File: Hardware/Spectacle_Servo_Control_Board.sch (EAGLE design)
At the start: 39 parts, among them J1 FTDI_DEVICE, J10 AUDIO-JACK3, J3 USB-MICROB, J4 AUDIO-JACK3, U1 CY8C4146LQI-S422, U2 3.3V/150mA

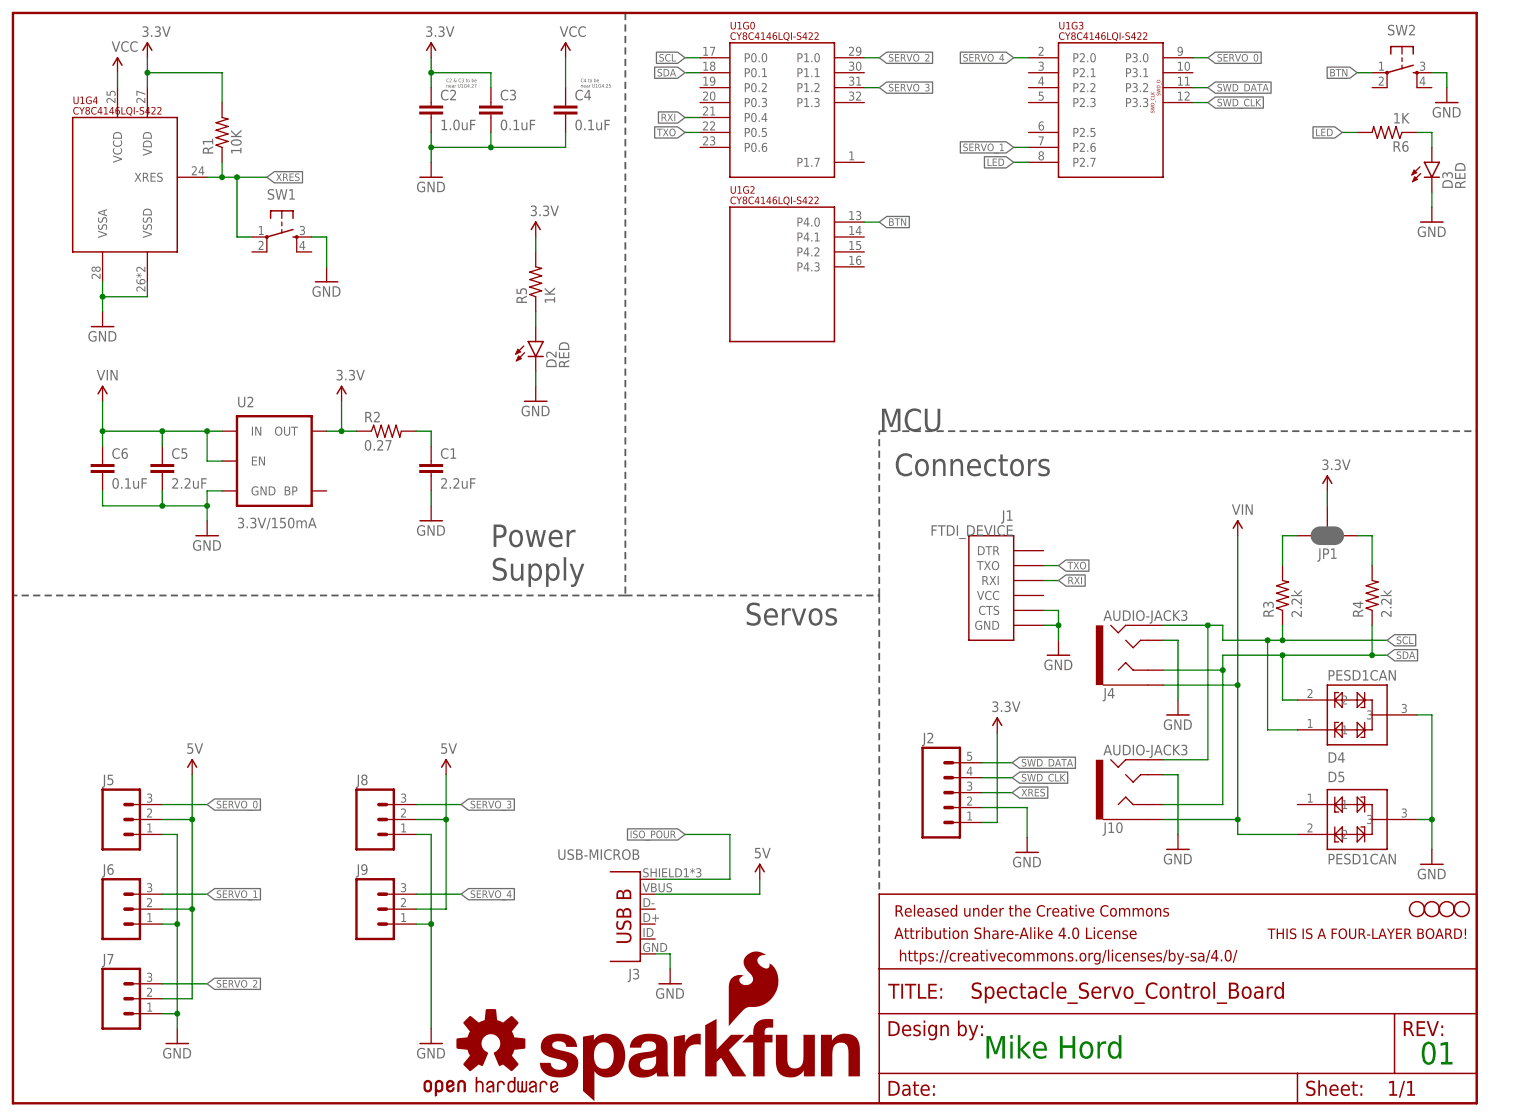
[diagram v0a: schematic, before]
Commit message: Changes from design review, initial checklist pass
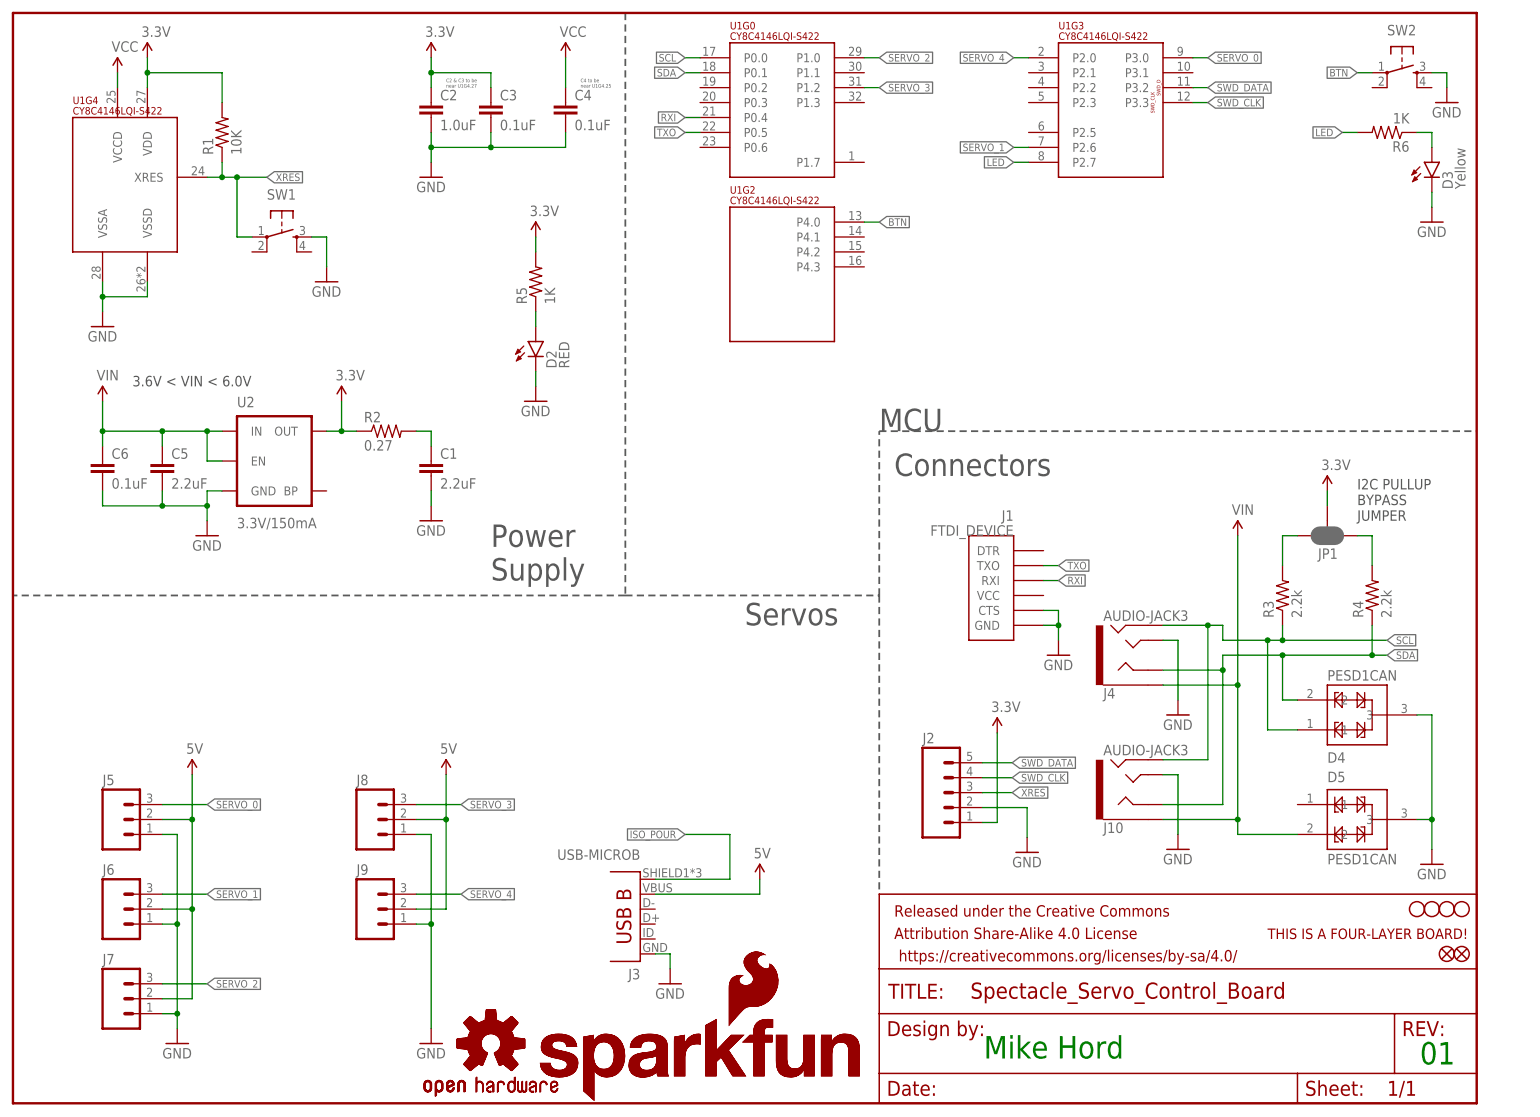
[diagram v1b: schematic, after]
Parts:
- added FD1, FD2: FIDUCIALUFIDUCIAL, SparkFun-Aesthetics:FIDUCIALUFIDUCIAL
- added LOGO3: SFE_LOGO_NAME_FLAME.1_INCH, SparkFun-Aesthetics:SFE_LOGO_NAME_FLAME.1_INCH
- added LOGO4: OSHW-LOGOS, SparkFun-Aesthetics:OSHW-LOGOS
- D3: value RED -> Yellow; device SparkFun-LED:LED-RED0603 -> SparkFun-LED:LED-YELLOW0603-SMART
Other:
- note added: "3.6V < VIN < 6.0V"
- note added: "I2C PULLUP BYPASS JUMPER"
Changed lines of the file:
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@@
 <part name="SW1" library="SparkFun-Electromechanical" deviceset="SWITCH_SPST_4_PIN" device="RECT"/>
 <part name="SW2" library="SparkFun-Electromechanical" deviceset="SWITCH_SPST_4_PIN" device="RECT"/>
-<part name="D3" library="SparkFun-LED" deviceset="LED-RED" device="0603" value="RED"/>
+<part name="D3" library="SparkFun-LED" deviceset="LED-YELLOW" device="0603-SMART" value="Yellow"/>
 <part name="R5" library="SparkFun-Resistors" deviceset="1KOHM-1/10W-1%(0603)" device="" value="1K"/>
 <part name="GND12" library="SparkFun-Aesthetics" deviceset="GND" device=""/>
@@
 <part name="J10" library="SparkFun-Connectors" deviceset="AUDIO-JACK3" device=""/>
 <part name="GND16" library="SparkFun-Aesthetics" deviceset="GND" device=""/>
+<part name="LOGO3" library="SparkFun-Aesthetics" deviceset="SFE_LOGO_NAME_FLAME" device=".1_INCH"/>
+<part name="LOGO4" library="SparkFun-Aesthetics" deviceset="OSHW-LOGO" device="S"/>
+<part name="FD1" library="SparkFun-Aesthetics" deviceset="FIDUCIAL" device="UFIDUCIAL"/>
+<part name="FD2" library="SparkFun-Aesthetics" deviceset="FIDUCIAL" device="UFIDUCIAL"/>
 </parts>
 <sheets>
@@
 <text x="81.28" y="88.9" size="3.81" layer="97" font="vector">Power
 Supply</text>
+<text x="20.32" y="121.92" size="1.778" layer="97">3.6V &lt; VIN &lt; 6.0V</text>
+<text x="228.6" y="99.06" size="1.778" layer="97">I2C PULLUP
+BYPASS
+JUMPER</text>
 </plain>
 <instances>
@@
 <instance part="J10" gate="G$1" x="190.5" y="53.34" rot="MR180"/>
 <instance part="GND16" gate="1" x="198.12" y="43.18"/>
+<instance part="LOGO3" gate="G$1" x="88.9" y="0"/>
+<instance part="LOGO4" gate="G$1" x="81.28" y="10.16"/>
+<instance part="FD1" gate="G$1" x="246.38" y="25.4"/>
+<instance part="FD2" gate="G$1" x="243.84" y="25.4"/>
 </instances>
 <busses>

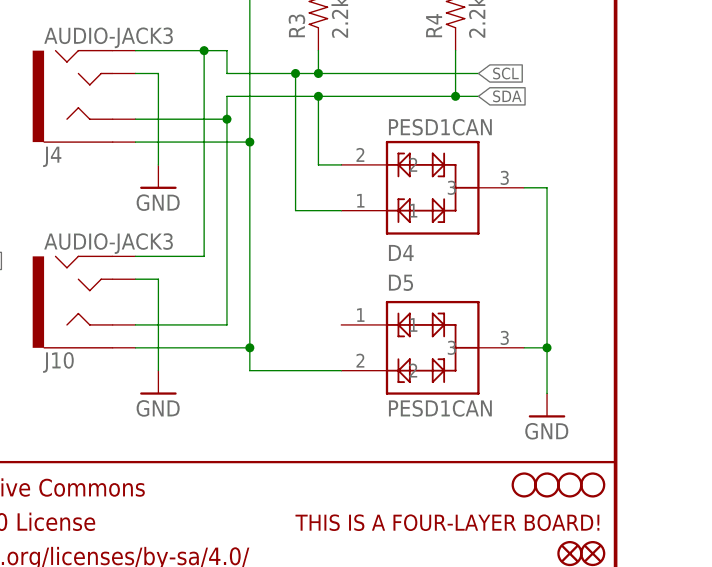
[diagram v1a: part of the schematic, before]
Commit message: Revised from feedback from QC
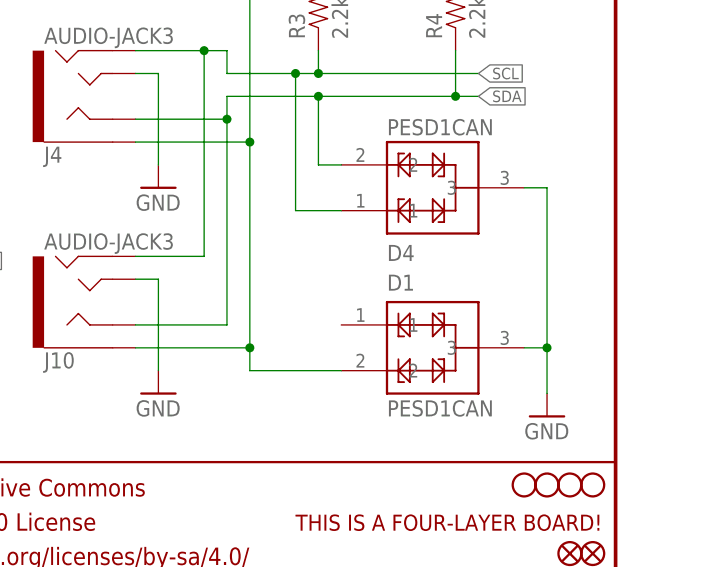
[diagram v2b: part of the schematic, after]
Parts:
- J10, J4: PROD_ID (none) -> CONN-10676
- renumbered D5 to D1
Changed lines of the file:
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@@
 <part name="SUPPLY9" library="SparkFun-Aesthetics" deviceset="3.3V" device=""/>
 <part name="SUPPLY11" library="SparkFun-Aesthetics" deviceset="3.3V" device=""/>
-<part name="J4" library="SparkFun-Connectors" deviceset="AUDIO-JACK3" device=""/>
+<part name="J4" library="SparkFun-Connectors" deviceset="AUDIO-JACK3" device="">
+<attribute name="PROD_ID" value="CONN-10676"/>
+</part>
 <part name="D4" library="SparkFun-DiscreteSemi" deviceset="PESD1CAN" device=""/>
 <part name="GND4" library="SparkFun-Aesthetics" deviceset="GND" device=""/>
-<part name="D5" library="SparkFun-DiscreteSemi" deviceset="PESD1CAN" device=""/>
+<part name="D1" library="SparkFun-DiscreteSemi" deviceset="PESD1CAN" device=""/>
 <part name="SUPPLY1" library="SparkFun-Aesthetics" deviceset="3.3V" device=""/>
 <part name="H1" library="SparkFun-Electromechanical" deviceset="STAND-OFF" device=""/>
@@
 <part name="LOGO1" library="SparkFun-Aesthetics" deviceset="OSHW-LOGO" device="S"/>
 <part name="LOGO2" library="SparkFun-Aesthetics" deviceset="SFE_LOGO_NAME_FLAME" device=".1_INCH"/>
-<part name="J10" library="SparkFun-Connectors" deviceset="AUDIO-JACK3" device=""/>
+<part name="J10" library="SparkFun-Connectors" deviceset="AUDIO-JACK3" device="">
+<attribute name="PROD_ID" value="CONN-10676"/>
+</part>
 <part name="GND16" library="SparkFun-Aesthetics" deviceset="GND" device=""/>
 <part name="LOGO3" library="SparkFun-Aesthetics" deviceset="SFE_LOGO_NAME_FLAME" device=".1_INCH"/>
@@
 <instance part="SUPPLY9" gate="G$1" x="55.88" y="119.38"/>
 <instance part="SUPPLY11" gate="G$1" x="223.52" y="104.14"/>
-<instance part="J4" gate="G$1" x="190.5" y="76.2" rot="MR180"/>
+<instance part="J4" gate="G$1" x="190.5" y="76.2" rot="MR180">
+<attribute name="PROD_ID" x="190.5" y="76.2" size="1.778" layer="96" rot="MR180" display="off"/>
+</instance>
 <instance part="D4" gate="G$1" x="223.52" y="71.12" rot="MR180"/>
 <instance part="GND4" gate="1" x="241.3" y="40.64"/>
-<instance part="D5" gate="G$1" x="223.52" y="43.18"/>
+<instance part="D1" gate="G$1" x="223.52" y="43.18"/>
 <instance part="SUPPLY1" gate="G$1" x="22.86" y="177.8"/>
 <instance part="H1" gate="G$1" x="246.38" y="33.02"/>
@@
 <instance part="LOGO1" gate="G$1" x="81.28" y="10.16"/>
 <instance part="LOGO2" gate="G$1" x="88.9" y="0"/>
-<instance part="J10" gate="G$1" x="190.5" y="53.34" rot="MR180"/>
+<instance part="J10" gate="G$1" x="190.5" y="53.34" rot="MR180">
+<attribute name="PROD_ID" x="190.5" y="53.34" size="1.778" layer="96" rot="MR180" display="off"/>
+</instance>
 <instance part="GND16" gate="1" x="198.12" y="43.18"/>
 <instance part="LOGO3" gate="G$1" x="88.9" y="0"/>
@@
 <wire x1="238.76" y1="66.04" x2="241.3" y2="66.04" width="0.1524" layer="91"/>
 <wire x1="241.3" y1="66.04" x2="241.3" y2="48.26" width="0.1524" layer="91"/>
-<pinref part="D5" gate="G$1" pin="3"/>
+<pinref part="D1" gate="G$1" pin="3"/>
 <wire x1="241.3" y1="48.26" x2="241.3" y2="43.18" width="0.1524" layer="91"/>
 <wire x1="238.76" y1="48.26" x2="241.3" y2="48.26" width="0.1524" layer="91"/>
@@
 <wire x1="208.28" y1="45.72" x2="208.28" y2="48.26" width="0.1524" layer="91"/>
 <junction x="208.28" y="71.12"/>
-<pinref part="D5" gate="G$1" pin="2"/>
+<pinref part="D1" gate="G$1" pin="2"/>
 <wire x1="208.28" y1="48.26" x2="208.28" y2="71.12" width="0.1524" layer="91"/>
 <wire x1="208.28" y1="45.72" x2="218.44" y2="45.72" width="0.1524" layer="91"/>

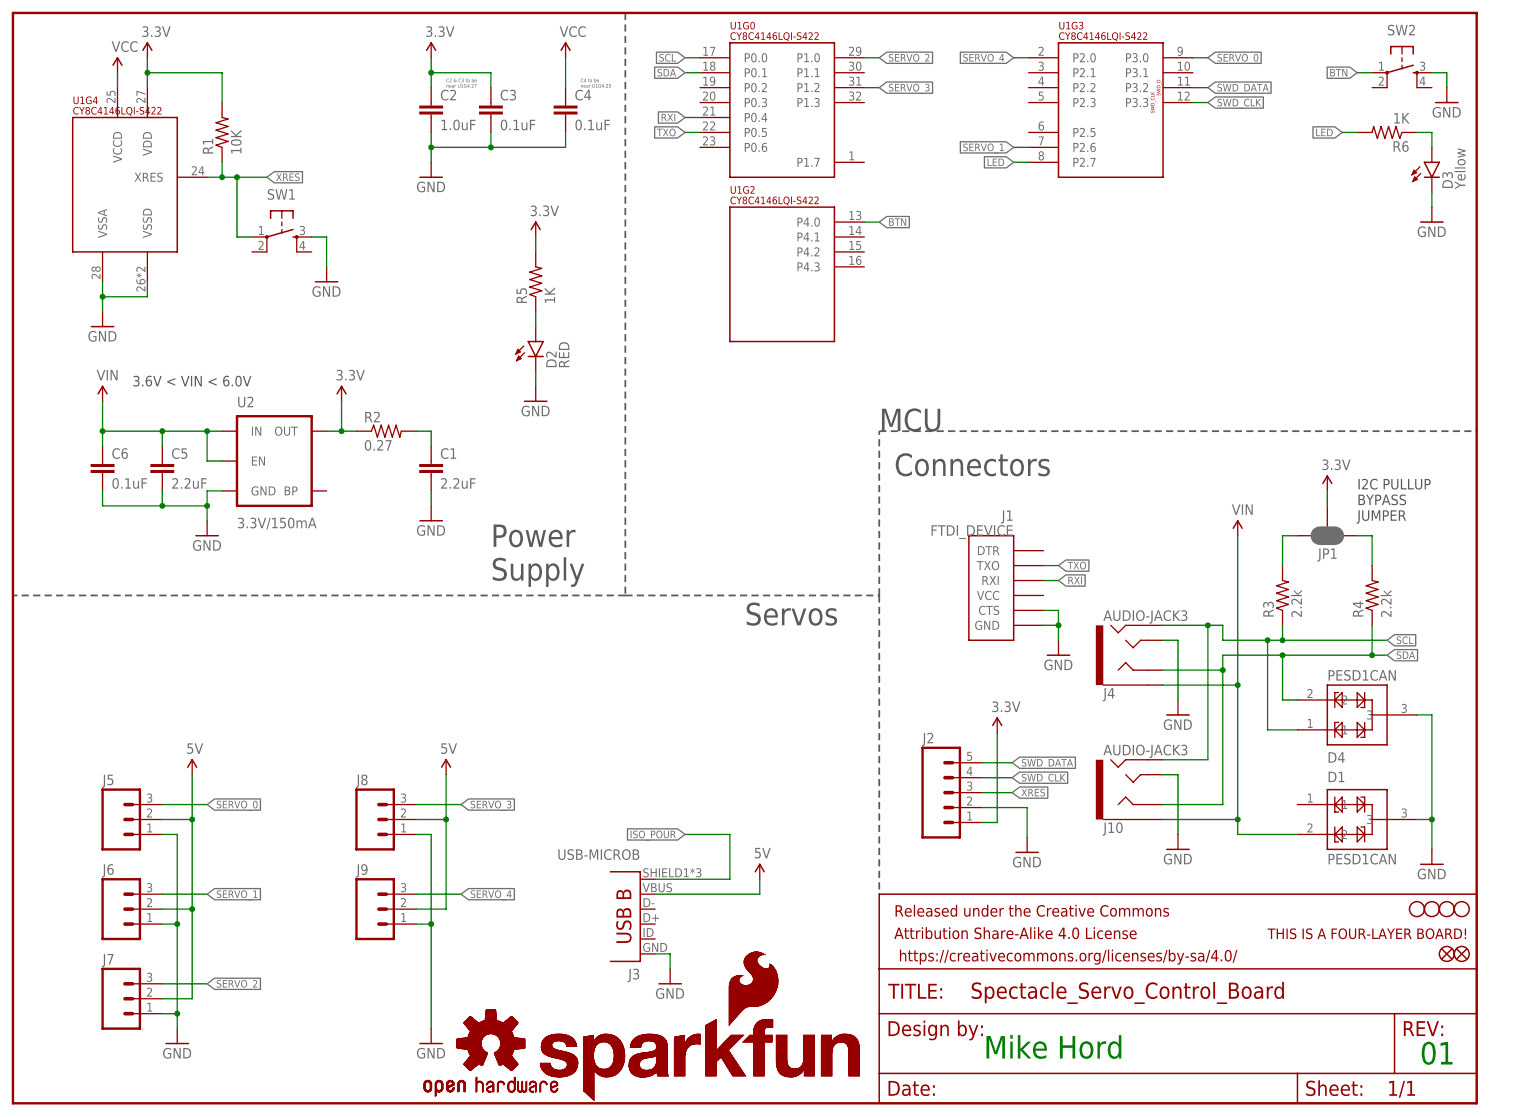
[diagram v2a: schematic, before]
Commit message: Added downstream power control circuitry
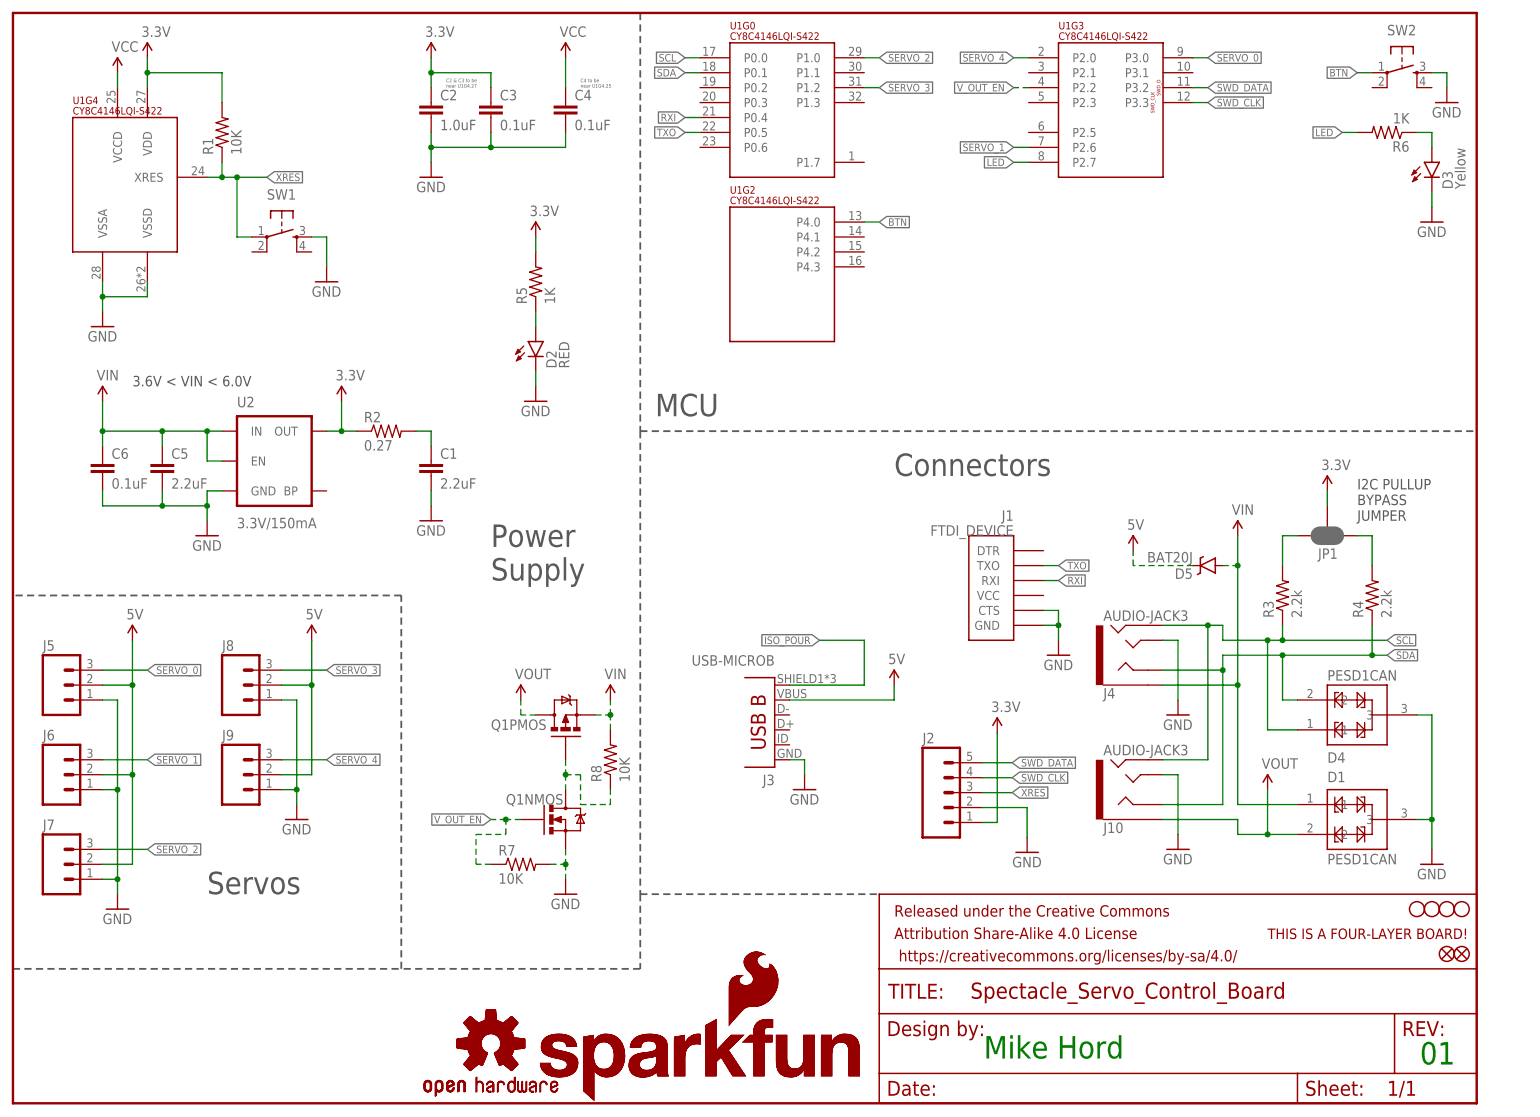
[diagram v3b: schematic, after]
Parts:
- added D5: BAT20J, SparkFun-DiscreteSemi:DIODE-SCHOTTKY-BAT20J
- added Q1: (no value), SparkFun-DiscreteSemi:IRF7509
- added R7, R8: 10K, SparkFun-Resistors:10KOHM-1/10W-1%(0603)0603
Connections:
- new net N$26: Q1NMOS.D, Q1PMOS.G, R8.1
- new net VOUT: D1.2, J10.EARTH, Q1PMOS.D
- new net V_OUT_EN: Q1NMOS.G, R7.1, U1G3.P2.2
- net 5V: now also D5.C
- net GND: now also Q1NMOS.S, R7.2
- net VIN: now also D1.1, D5.A, Q1PMOS.S, R8.2; no longer D1.2, J10.EARTH
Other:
- moved on the sheet: J3, J5, J6, J7, J8, J9
